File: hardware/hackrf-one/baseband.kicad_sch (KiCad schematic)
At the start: 136 parts, among them P14 XCVR_CLKOUT, P15 INTR, P16 CLKIN, P18 OEB, P2 CLKOUT, P37 SCL, P38 SDA, P39 SSP1_SCK, P40 SSP1_COPI, P41 SSP1_CIPO, P53 CS_XCVR, P54 CS_AD, P55 TXENABLE, P56 RXENABLE, P57 XTAL2, P58 GCK1, P59 GCK2, P60 SGPIO_CLK, P61 DA0, P62 DA7, P63 DD0, P64 DD9, P65 DA4, P66 DD5, P67 RSSI, P83 GND, P84 GND, P85 GND, P86 GND, P87 GND, P88 GND, P89 GND, P9 BASEBAND, P90 GND, P91 GND, P92 GND, Q3 MOSFET_P, T3 RX_BALUN, T4 TX_BALUN, U17 MAX2837, U18 MAX5864, U19 SI5351C, X1 GSG-XTAL4PIN

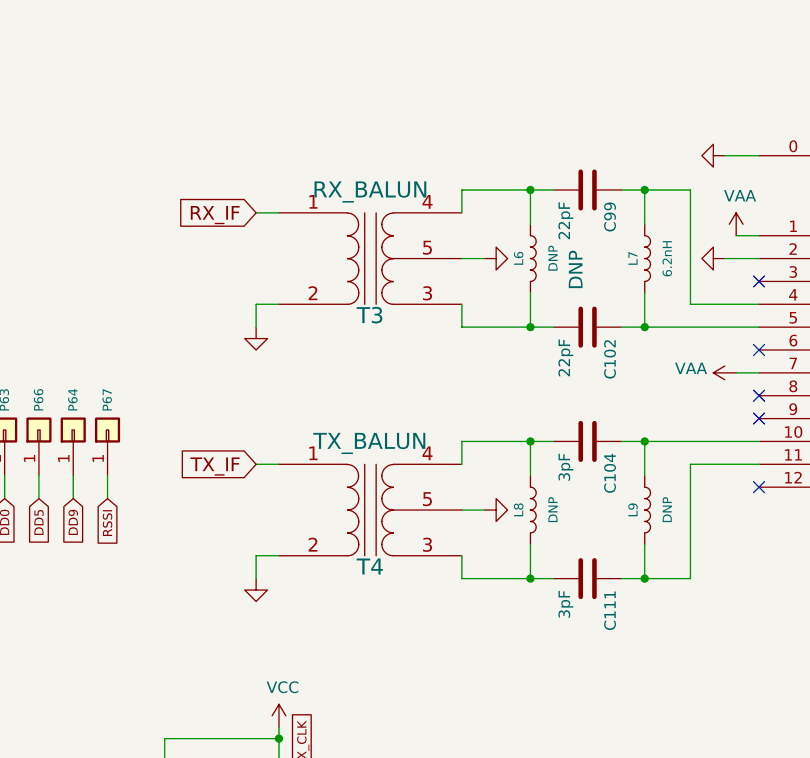
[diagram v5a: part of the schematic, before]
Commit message: HackRF One: correct T3 and T4 balun symbol
- Swap GND pins to reflect correct internal wiring
- Remove obsolete and apparently incorrect substitution
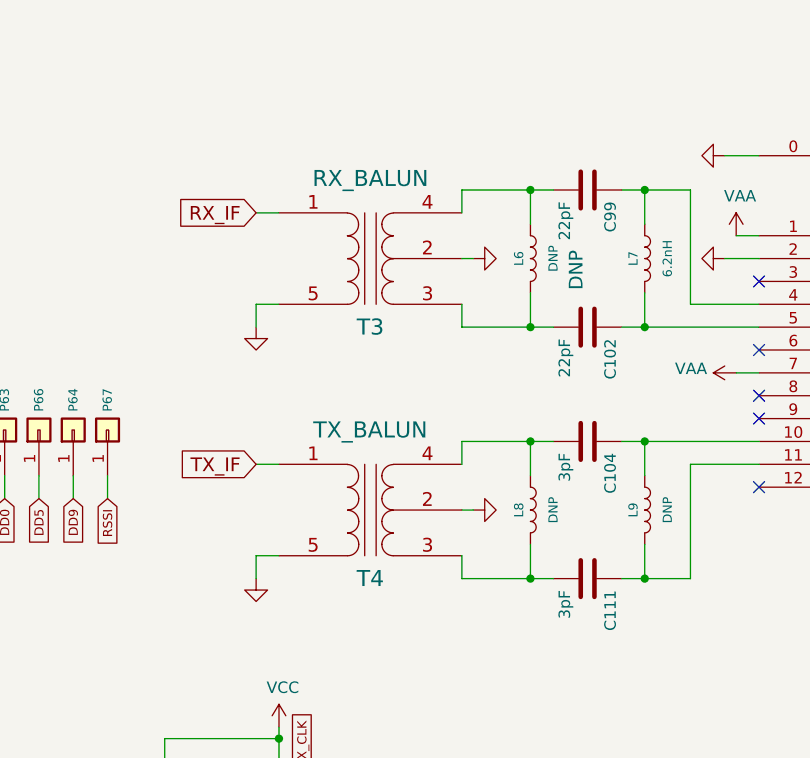
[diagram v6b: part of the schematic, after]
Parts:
- T3, T4: symbol gsg-symbols:BALUN -> hackrf:BALUN-2500BL14M100T; Substitution Murata LDB182G4510G-120 -> (none)
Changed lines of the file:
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@@
     (stroke (width 0) (type default) (color 0 0 0 0))
   )
-  (wire (pts (xy 132.08 114.3) (xy 129.54 114.3))
+  (wire (pts (xy 130.81 114.3) (xy 129.54 114.3))
     (stroke (width 0) (type default) (color 0 0 0 0))
   )
@@
     (stroke (width 0) (type default) (color 0 0 0 0))
   )
-  (wire (pts (xy 132.08 142.24) (xy 129.54 142.24))
+  (wire (pts (xy 130.81 142.24) (xy 129.54 142.24))
     (stroke (width 0) (type default) (color 0 0 0 0))
   )
@@
     (pin "2")
   )
-  (symbol (lib_id "gsg-symbols:BALUN") (at 119.38 114.3 180) (unit 1)
-    (in_bom yes) (on_board yes)
-    (property "Reference" "T3" (id 0) (at 119.38 120.65 0)
+  (symbol (lib_id "hackrf:BALUN-2500BL14M100T") (at 119.38 114.3 180) (unit 1)
+    (in_bom yes) (on_board yes)
+    (property "Reference" "T3" (id 0) (at 119.38 121.92 0)
       (effects (font (size 1.778 1.778)))
     )
-    (property "Value" "RX_BALUN" (id 1) (at 119.38 106.68 0)
+    (property "Value" "RX_BALUN" (id 1) (at 119.38 105.41 0)
       (effects (font (size 1.778 1.778)))
     )
@@
       (effects (font (size 1.524 1.524)) hide)
     )
-    (property "Substitution" "Murata LDB182G4510G-120" (id 7) (at 119.38 114.3 0)
+    (property "Substitution" "" (id 7) (at 119.38 114.3 0)
       (effects (font (size 1.27 1.27)) hide)
     )
@@
     (pin "5")
   )
-  (symbol (lib_id "power:GND") (at 132.08 114.3 90) (unit 1)
-    (in_bom yes) (on_board yes)
-    (property "Reference" "#PWR0139" (id 0) (at 132.08 114.3 0)
-      (effects (font (size 0.762 0.762)) hide)
-    )
-    (property "Value" "GND" (id 1) (at 133.858 114.3 0)
-      (effects (font (size 0.762 0.762)) hide)
-    )
-    (property "Footprint" "" (id 2) (at 132.08 114.3 0)
-      (effects (font (size 1.524 1.524)) hide)
-    )
-    (property "Datasheet" "" (id 3) (at 132.08 114.3 0)
-      (effects (font (size 1.524 1.524)) hide)
-    )
-    (pin "1")
-  )
-  (symbol (lib_id "power:GND") (at 132.08 142.24 90) (unit 1)
-    (in_bom yes) (on_board yes)
-    (property "Reference" "#PWR0138" (id 0) (at 132.08 142.24 0)
-      (effects (font (size 0.762 0.762)) hide)
-    )
-    (property "Value" "GND" (id 1) (at 133.858 142.24 0)
-      (effects (font (size 0.762 0.762)) hide)
-    )
-    (property "Footprint" "" (id 2) (at 132.08 142.24 0)
-      (effects (font (size 1.524 1.524)) hide)
-    )
-    (property "Datasheet" "" (id 3) (at 132.08 142.24 0)
-      (effects (font (size 1.524 1.524)) hide)
-    )
-    (pin "1")
-  )
-  (symbol (lib_id "gsg-symbols:BALUN") (at 119.38 142.24 180) (unit 1)
-    (in_bom yes) (on_board yes)
-    (property "Reference" "T4" (id 0) (at 119.38 148.59 0)
+  (symbol (lib_id "power:GND") (at 130.81 114.3 90) (unit 1)
+    (in_bom yes) (on_board yes)
+    (property "Reference" "#PWR0139" (id 0) (at 130.81 114.3 0)
+      (effects (font (size 0.762 0.762)) hide)
+    )
+    (property "Value" "GND" (id 1) (at 132.588 114.3 0)
+      (effects (font (size 0.762 0.762)) hide)
+    )
+    (property "Footprint" "" (id 2) (at 130.81 114.3 0)
+      (effects (font (size 1.524 1.524)) hide)
+    )
+    (property "Datasheet" "" (id 3) (at 130.81 114.3 0)
+      (effects (font (size 1.524 1.524)) hide)
+    )
+    (pin "1")
+  )
+  (symbol (lib_id "power:GND") (at 130.81 142.24 90) (unit 1)
+    (in_bom yes) (on_board yes)
+    (property "Reference" "#PWR0138" (id 0) (at 130.81 142.24 0)
+      (effects (font (size 0.762 0.762)) hide)
+    )
+    (property "Value" "GND" (id 1) (at 132.588 142.24 0)
+      (effects (font (size 0.762 0.762)) hide)
+    )
+    (property "Footprint" "" (id 2) (at 130.81 142.24 0)
+      (effects (font (size 1.524 1.524)) hide)
+    )
+    (property "Datasheet" "" (id 3) (at 130.81 142.24 0)
+      (effects (font (size 1.524 1.524)) hide)
+    )
+    (pin "1")
+  )
+  (symbol (lib_id "hackrf:BALUN-2500BL14M100T") (at 119.38 142.24 180) (unit 1)
+    (in_bom yes) (on_board yes)
+    (property "Reference" "T4" (id 0) (at 119.38 149.86 0)
       (effects (font (size 1.778 1.778)))
     )
-    (property "Value" "TX_BALUN" (id 1) (at 119.38 134.62 0)
+    (property "Value" "TX_BALUN" (id 1) (at 119.38 133.35 0)
       (effects (font (size 1.778 1.778)))
     )
@@
       (effects (font (size 1.524 1.524)) hide)
     )
-    (property "Substitution" "Murata LDB182G4510G-120" (id 7) (at 119.38 142.24 0)
-      (effects (font (size 1.27 1.27)) hide)
-    )
+    (property "Substitution" "" (id 7) (at 119.38 142.24 0)
+      (effects (font (size 1.27 1.27)) hide)
+    )

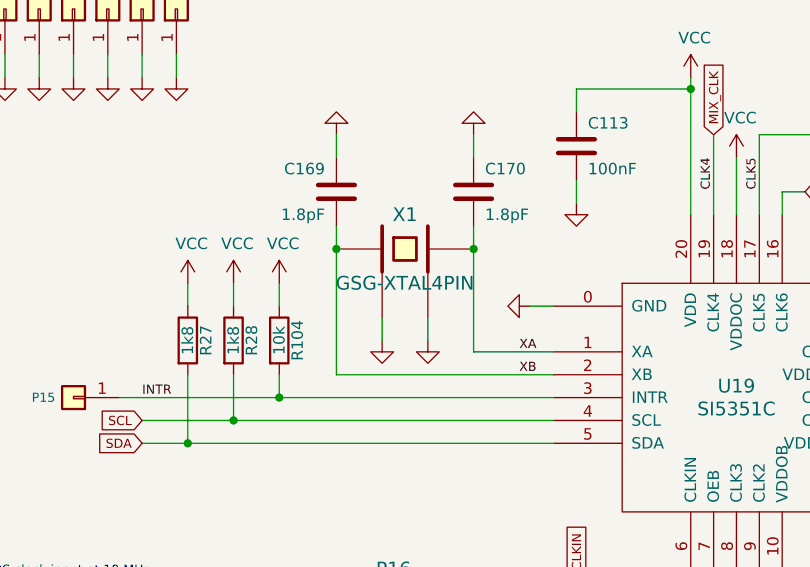
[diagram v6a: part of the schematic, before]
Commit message: HackRF One: clean up symbol value names
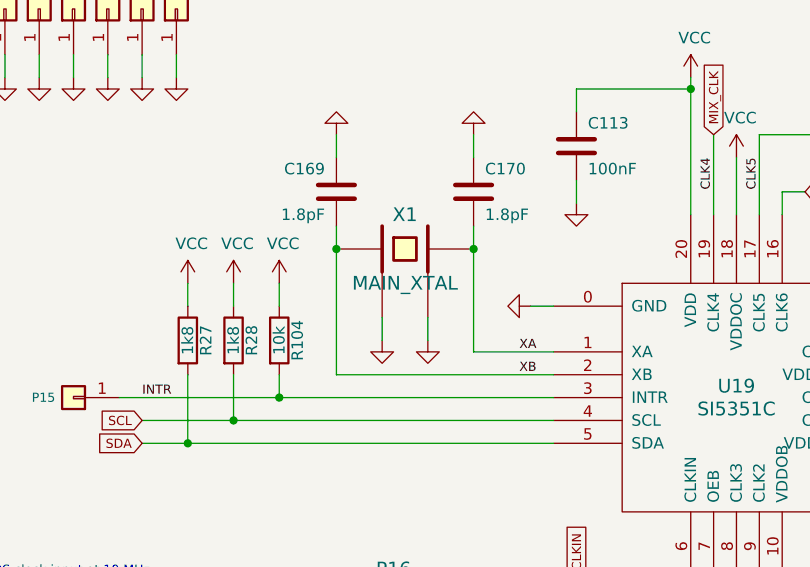
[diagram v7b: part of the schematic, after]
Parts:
- X1: value GSG-XTAL4PIN -> MAIN_XTAL
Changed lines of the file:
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@@
       (effects (font (size 1.524 1.524)))
     )
-    (property "Value" "GSG-XTAL4PIN" (id 1) (at 77.47 189.23 0)
+    (property "Value" "MAIN_XTAL" (id 1) (at 77.47 189.23 0)
       (effects (font (size 1.524 1.524)))
     )

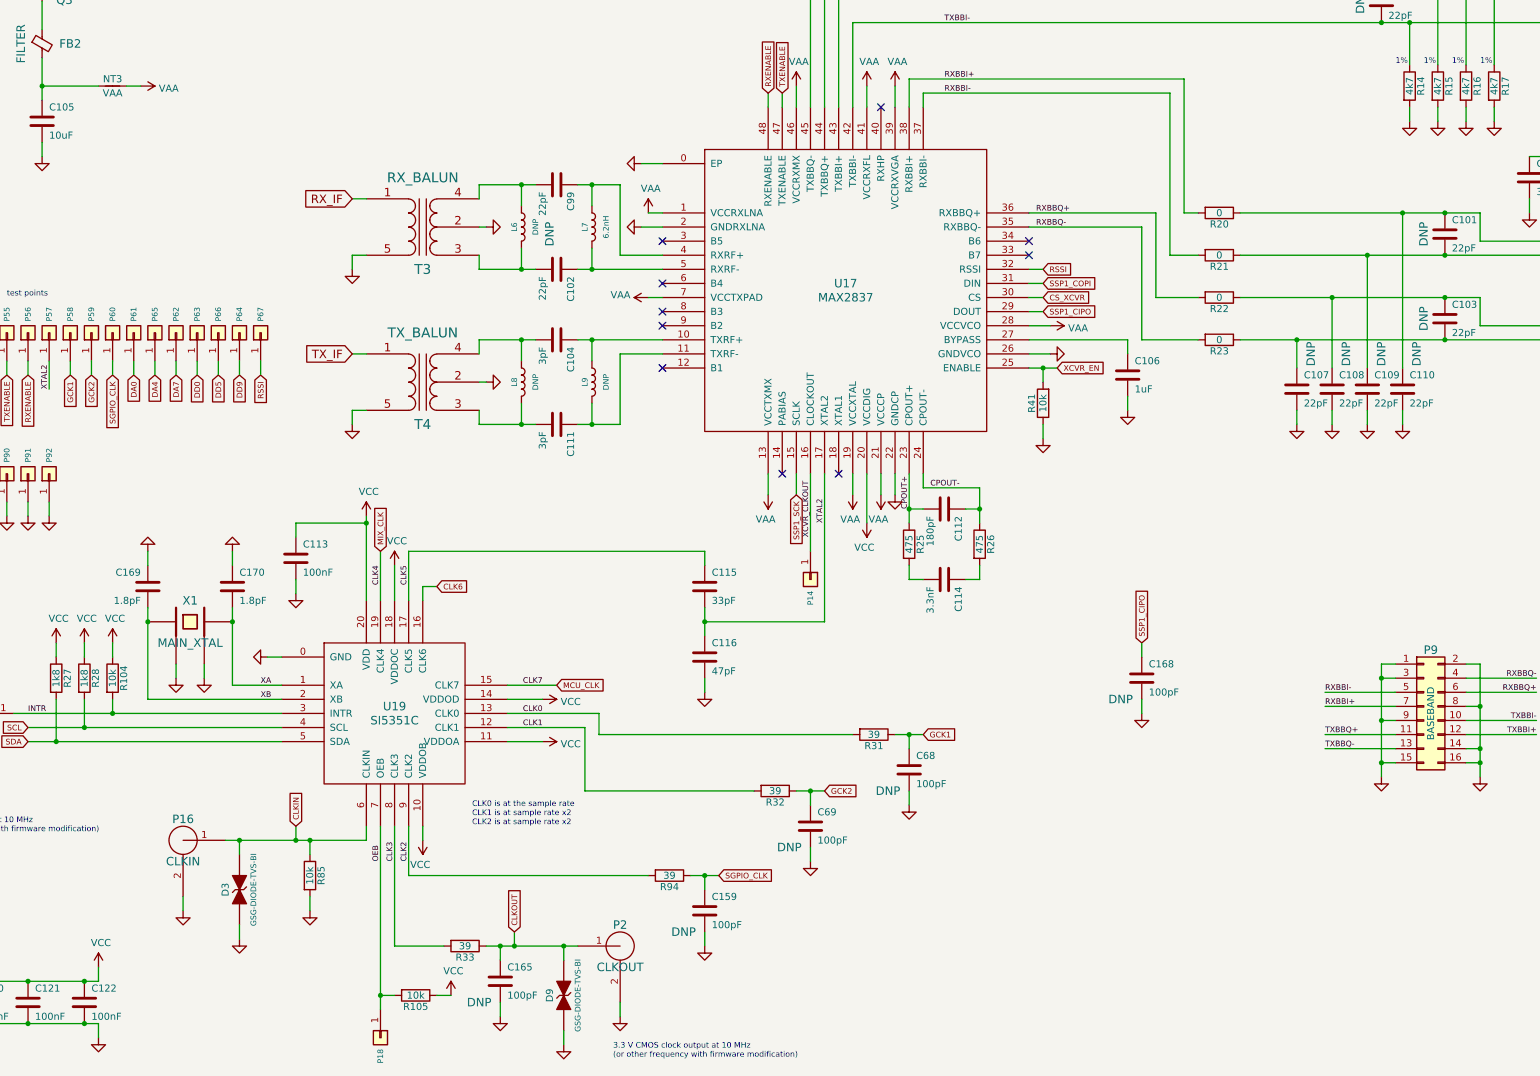
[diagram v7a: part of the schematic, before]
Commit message: HackRF One: correct fabrication attributes and DNP
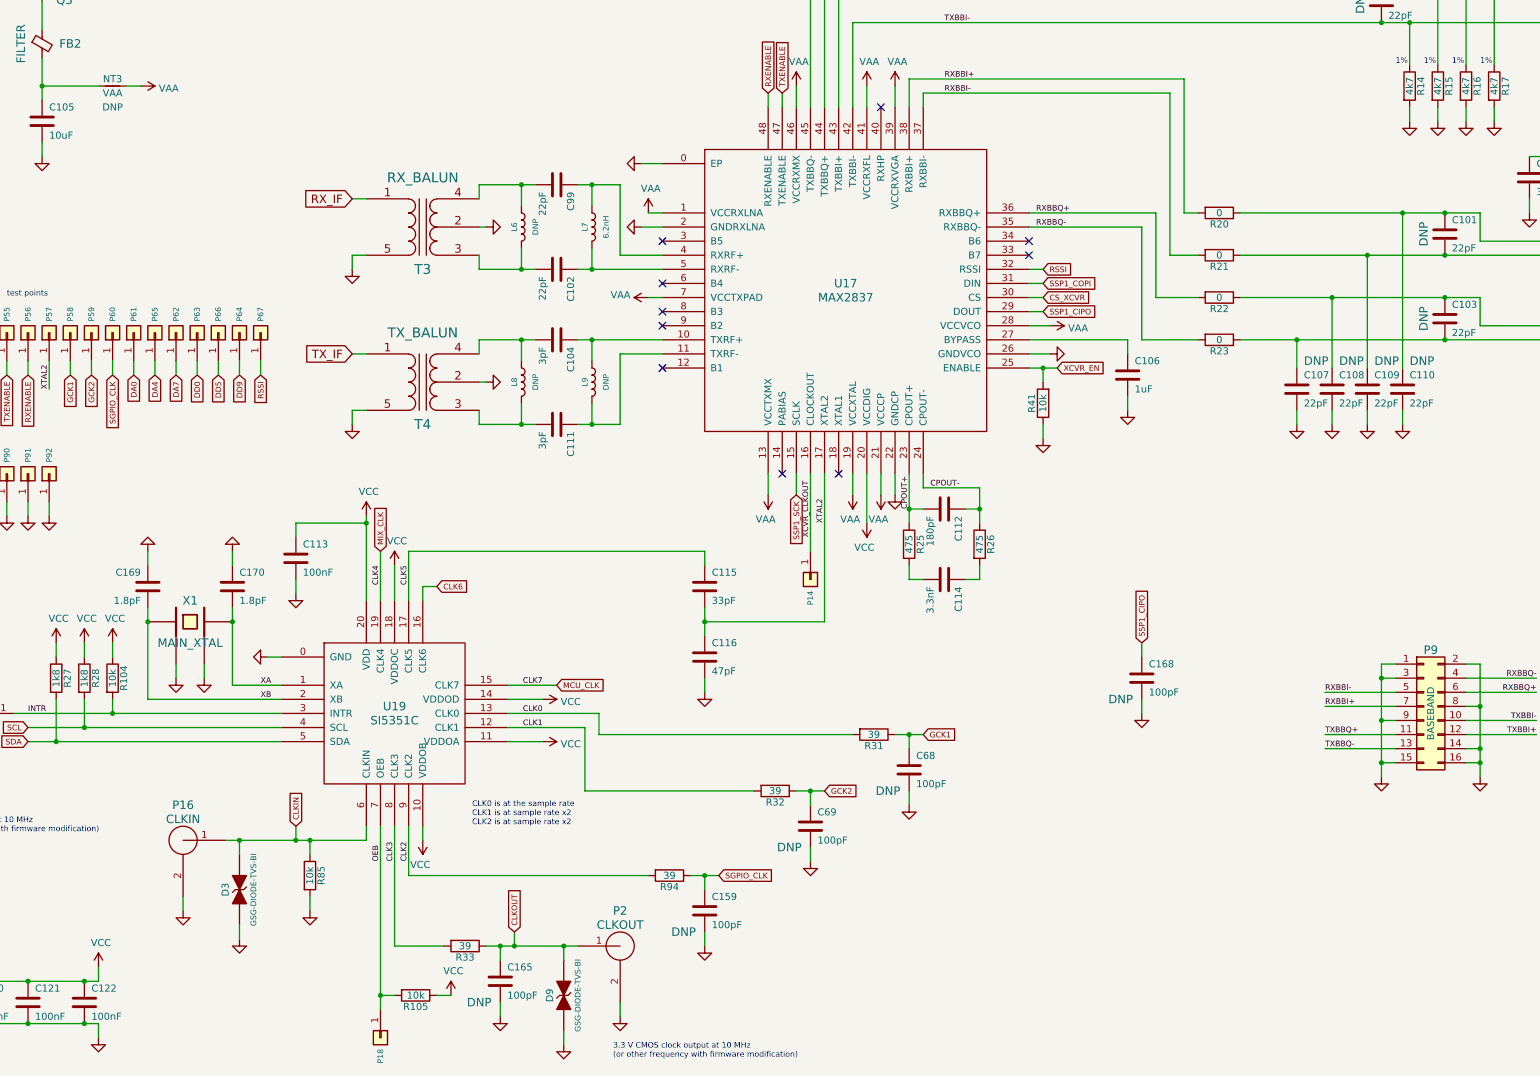
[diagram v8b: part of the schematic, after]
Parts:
- P14, P15, P18, P37, P38, P39, P40, P41, P53, P54, P55, P56, P57, P58, P59, P60, P61, P62, P63, P64, P65, P66, P67, P83, P84, P85, P86, P87, P88, P89, P90, P91, P92: DNP DNP -> (none); now left out of the parts list
